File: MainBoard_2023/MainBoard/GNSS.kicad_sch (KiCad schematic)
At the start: 13 parts

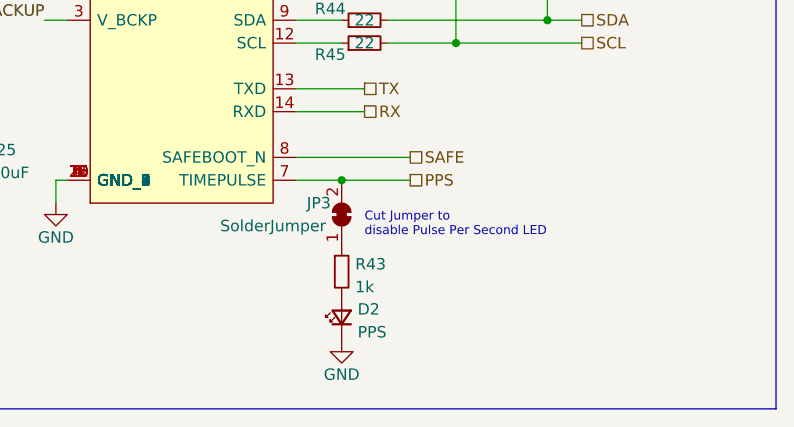
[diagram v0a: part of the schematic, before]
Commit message: 配線のこり半分
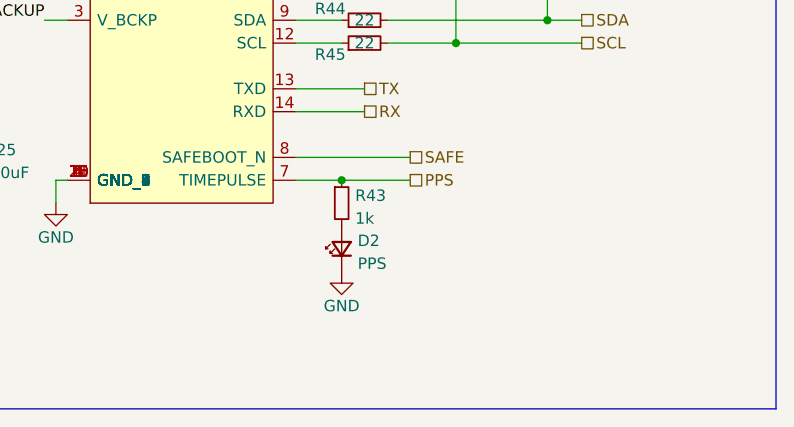
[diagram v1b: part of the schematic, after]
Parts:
- removed JP3: SolderJumper, Jumper:SolderJumper-2_P1.3mm_Open_TrianglePad1.0x1.5mm, symbol Jumper:SolderJumper_2_Bridged
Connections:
- net PPS: now also R43.1
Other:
- note removed: "Cut Jumper to disable Pulse Per Second LED"
- moved on the sheet: D2, R43
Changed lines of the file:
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@@
 (kicad_sch (version 20211123) (generator eeschema)
   (paper "A4")
+  (junction (at 177.8 104.14) (diameter 0) (color 0 0 0 0)
+  )
   (junction (at 146.05 78.74) (diameter 0) (color 0 0 0 0)
   )
@@
   (junction (at 102.87 80.01) (diameter 0) (color 0 0 0 0)
   )
-  (junction (at 177.8 104.14) (diameter 0) (color 0 0 0 0)
-  )
   (wire (pts (xy 147.32 86.36) (xy 144.78 86.36))
     (stroke (width 0) (type default) (color 0 0 0 0))
@@
     (stroke (width 0) (type default) (color 0 0 0 0))
   )
+  (wire (pts (xy 177.8 104.14) (xy 185.42 104.14))
+    (stroke (width 0) (type default) (color 0 0 0 0))
+  )
   (wire (pts (xy 146.05 76.2) (xy 146.05 78.74))
     (stroke (width 0) (type default) (color 0 0 0 0))
@@
     (stroke (width 0) (type default) (color 0 0 0 0))
   )
+  (polyline (pts (xy 67.31 96.52) (xy 67.31 57.15))
+    (stroke (width 0) (type default) (color 0 0 0 0))
+  )
+  (polyline (pts (xy 226.06 57.15) (xy 226.06 129.54))
+    (stroke (width 0) (type default) (color 0 0 0 0))
+  )
+  (polyline (pts (xy 124.46 57.15) (xy 124.46 129.54))
+    (stroke (width 0) (type default) (color 0 0 0 0))
+  )
+  (wire (pts (xy 190.5 82.55) (xy 190.5 88.9))
+    (stroke (width 0) (type default) (color 0 0 0 0))
+  )
+  (wire (pts (xy 175.26 78.74) (xy 172.72 78.74))
+    (stroke (width 0) (type default) (color 0 0 0 0))
+  )
+  (wire (pts (xy 175.26 81.28) (xy 172.72 81.28))
+    (stroke (width 0) (type default) (color 0 0 0 0))
+  )
+  (wire (pts (xy 182.88 88.9) (xy 190.5 88.9))
+    (stroke (width 0) (type default) (color 0 0 0 0))
+  )
+  (polyline (pts (xy 226.06 129.54) (xy 124.46 129.54))
+    (stroke (width 0) (type default) (color 0 0 0 0))
+  )
+  (wire (pts (xy 172.72 93.98) (xy 180.34 93.98))
+    (stroke (width 0) (type default) (color 0 0 0 0))
+  )
   (wire (pts (xy 172.72 104.14) (xy 177.8 104.14))
-    (stroke (width 0) (type default) (color 0 0 0 0))
-  )
-  (polyline (pts (xy 67.31 96.52) (xy 67.31 57.15))
-    (stroke (width 0) (type default) (color 0 0 0 0))
-  )
-  (polyline (pts (xy 226.06 57.15) (xy 226.06 129.54))
-    (stroke (width 0) (type default) (color 0 0 0 0))
-  )
-  (polyline (pts (xy 124.46 57.15) (xy 124.46 129.54))
-    (stroke (width 0) (type default) (color 0 0 0 0))
-  )
-  (wire (pts (xy 190.5 82.55) (xy 190.5 88.9))
-    (stroke (width 0) (type default) (color 0 0 0 0))
-  )
-  (wire (pts (xy 175.26 78.74) (xy 172.72 78.74))
-    (stroke (width 0) (type default) (color 0 0 0 0))
-  )
-  (wire (pts (xy 175.26 81.28) (xy 172.72 81.28))
-    (stroke (width 0) (type default) (color 0 0 0 0))
-  )
-  (wire (pts (xy 182.88 88.9) (xy 190.5 88.9))
-    (stroke (width 0) (type default) (color 0 0 0 0))
-  )
-  (polyline (pts (xy 226.06 129.54) (xy 124.46 129.54))
-    (stroke (width 0) (type default) (color 0 0 0 0))
-  )
-  (wire (pts (xy 172.72 93.98) (xy 180.34 93.98))
-    (stroke (width 0) (type default) (color 0 0 0 0))
-  )
-  (wire (pts (xy 177.8 104.14) (xy 185.42 104.14))
     (stroke (width 0) (type default) (color 0 0 0 0))
   )
@@
     (effects (font (size 1 1)) (justify left bottom))
   )
-  (text "Cut Jumper to\ndisable Pulse Per Second LED" (at 180.34 110.49 180)
-    (effects (font (size 1 1)) (justify left bottom))
-  )
   (text "RTC Backup" (at 115.57 62.23 180)
     (effects (font (size 2.54 2.54)) (justify right bottom))
@@
     (pin "1")
   )
-  (symbol (lib_id "power:GND") (at 177.8 121.92 0) (unit 1)
-    (in_bom yes) (on_board yes)
-    (property "Reference" "#PWR0126" (id 0) (at 177.8 128.27 0)
-      (effects (font (size 1.27 1.27)) hide)
-    )
-    (property "Value" "GND" (id 1) (at 177.8 125.73 0))
-    (property "Footprint" "" (id 2) (at 177.8 121.92 0)
-      (effects (font (size 1.27 1.27)) hide)
-    )
-    (property "Datasheet" "" (id 3) (at 177.8 121.92 0)
+  (symbol (lib_id "power:GND") (at 177.8 114.3 0) (unit 1)
+    (in_bom yes) (on_board yes)
+    (property "Reference" "#PWR0126" (id 0) (at 177.8 120.65 0)
+      (effects (font (size 1.27 1.27)) hide)
+    )
+    (property "Value" "GND" (id 1) (at 177.8 118.11 0))
+    (property "Footprint" "" (id 2) (at 177.8 114.3 0)
+      (effects (font (size 1.27 1.27)) hide)
+    )
+    (property "Datasheet" "" (id 3) (at 177.8 114.3 0)
       (effects (font (size 1.27 1.27)) hide)
     )
@@
     (pin "1")
   )
-  (symbol (lib_id "Device:R_Small") (at 177.8 114.3 0) (unit 1)
+  (symbol (lib_id "Device:R_Small") (at 177.8 106.68 0) (unit 1)
     (in_bom yes) (on_board yes) (fields_autoplaced)
-    (property "Reference" "R43" (id 0) (at 179.2986 113.4653 0)
-      (effects (font (size 1.27 1.27)) (justify left))
-    )
-    (property "Value" "1k" (id 1) (at 179.2986 116.0022 0)
-      (effects (font (size 1.27 1.27)) (justify left))
-    )
-    (property "Footprint" "Resistor_SMD:R_0603_1608Metric_Pad0.98x0.95mm_HandSolder" (id 2) (at 177.8 114.3 0)
-      (effects (font (size 1.27 1.27)) hide)
-    )
-    (property "Datasheet" "~" (id 3) (at 177.8 114.3 0)
+    (property "Reference" "R43" (id 0) (at 179.2986 105.8453 0)
+      (effects (font (size 1.27 1.27)) (justify left))
+    )
+    (property "Value" "1k" (id 1) (at 179.2986 108.3822 0)
+      (effects (font (size 1.27 1.27)) (justify left))
+    )
+    (property "Footprint" "Resistor_SMD:R_0603_1608Metric_Pad0.98x0.95mm_HandSolder" (id 2) (at 177.8 106.68 0)
+      (effects (font (size 1.27 1.27)) hide)
+    )
+    (property "Datasheet" "~" (id 3) (at 177.8 106.68 0)
       (effects (font (size 1.27 1.27)) hide)
     )
@@
     (pin "2")
   )
-  (symbol (lib_id "Jumper:SolderJumper_2_Bridged") (at 177.8 107.95 90) (unit 1)
-    (in_bom yes) (on_board yes)
-    (property "Reference" "JP3" (id 0) (at 175.26 106.68 90))
-    (property "Value" "SolderJumper" (id 1) (at 170.18 109.22 90))
-    (property "Footprint" "Jumper:SolderJumper-2_P1.3mm_Open_TrianglePad1.0x1.5mm" (id 2) (at 177.8 107.95 0)
-      (effects (font (size 1.27 1.27)) hide)
-    )
-    (property "Datasheet" "~" (id 3) (at 177.8 107.95 0)
-      (effects (font (size 1.27 1.27)) hide)
-    )
-    (pin "1")
-    (pin "2")
-  )
   (symbol (lib_id "Device:R_Small") (at 190.5 80.01 180) (unit 1)
     (in_bom yes) (on_board yes)
@@
     (pin "1")
   )
-  (symbol (lib_id "Device:LED_Small") (at 177.8 119.38 90) (unit 1)
+  (symbol (lib_id "Device:LED_Small") (at 177.8 111.76 90) (unit 1)
     (in_bom yes) (on_board yes) (fields_autoplaced)
-    (property "Reference" "D2" (id 0) (at 179.578 118.4818 90)
+    (property "Reference" "D2" (id 0) (at 179.578 110.8618 90)
       (effects (font (size 1.27 1.27)) (justify right))
     )
-    (property "Value" "PPS" (id 1) (at 179.578 121.0187 90)
+    (property "Value" "PPS" (id 1) (at 179.578 113.3987 90)
       (effects (font (size 1.27 1.27)) (justify right))
     )
-    (property "Footprint" "LED_SMD:LED_1206_3216Metric_Pad1.42x1.75mm_HandSolder" (id 2) (at 177.8 119.38 90)
-      (effects (font (size 1.27 1.27)) hide)
-    )
-    (property "Datasheet" "~" (id 3) (at 177.8 119.38 90)
-      (effects (font (size 1.27 1.27)) hide)
-    )
+    (property "Footprint" "LED_SMD:LED_1206_3216Metric_Pad1.42x1.75mm_HandSolder" (id 2) (at 177.8 111.76 90)
+      (effects (font (size 1.27 1.27)) hide)
+    )
+    (property "Datasheet" "~" (id 3) (at 177.8 111.76 90)
+      (effects (font (size 1.27 1.27)) hide)
+    )
